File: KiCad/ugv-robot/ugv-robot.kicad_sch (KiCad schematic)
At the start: 16 parts, among them J1 Charging_Port, SW1 LRF, SW2 Zoom_In, SW3 Zoom_Out, SW4 Body_Up, SW5 Body_Down, SW6 Lamp, U1 Analog_Joystick, U2 Digital_Joystick, U3 Boost_Conv, U4 Asus_NUC, U6 Monitor, U7 USB_HUB

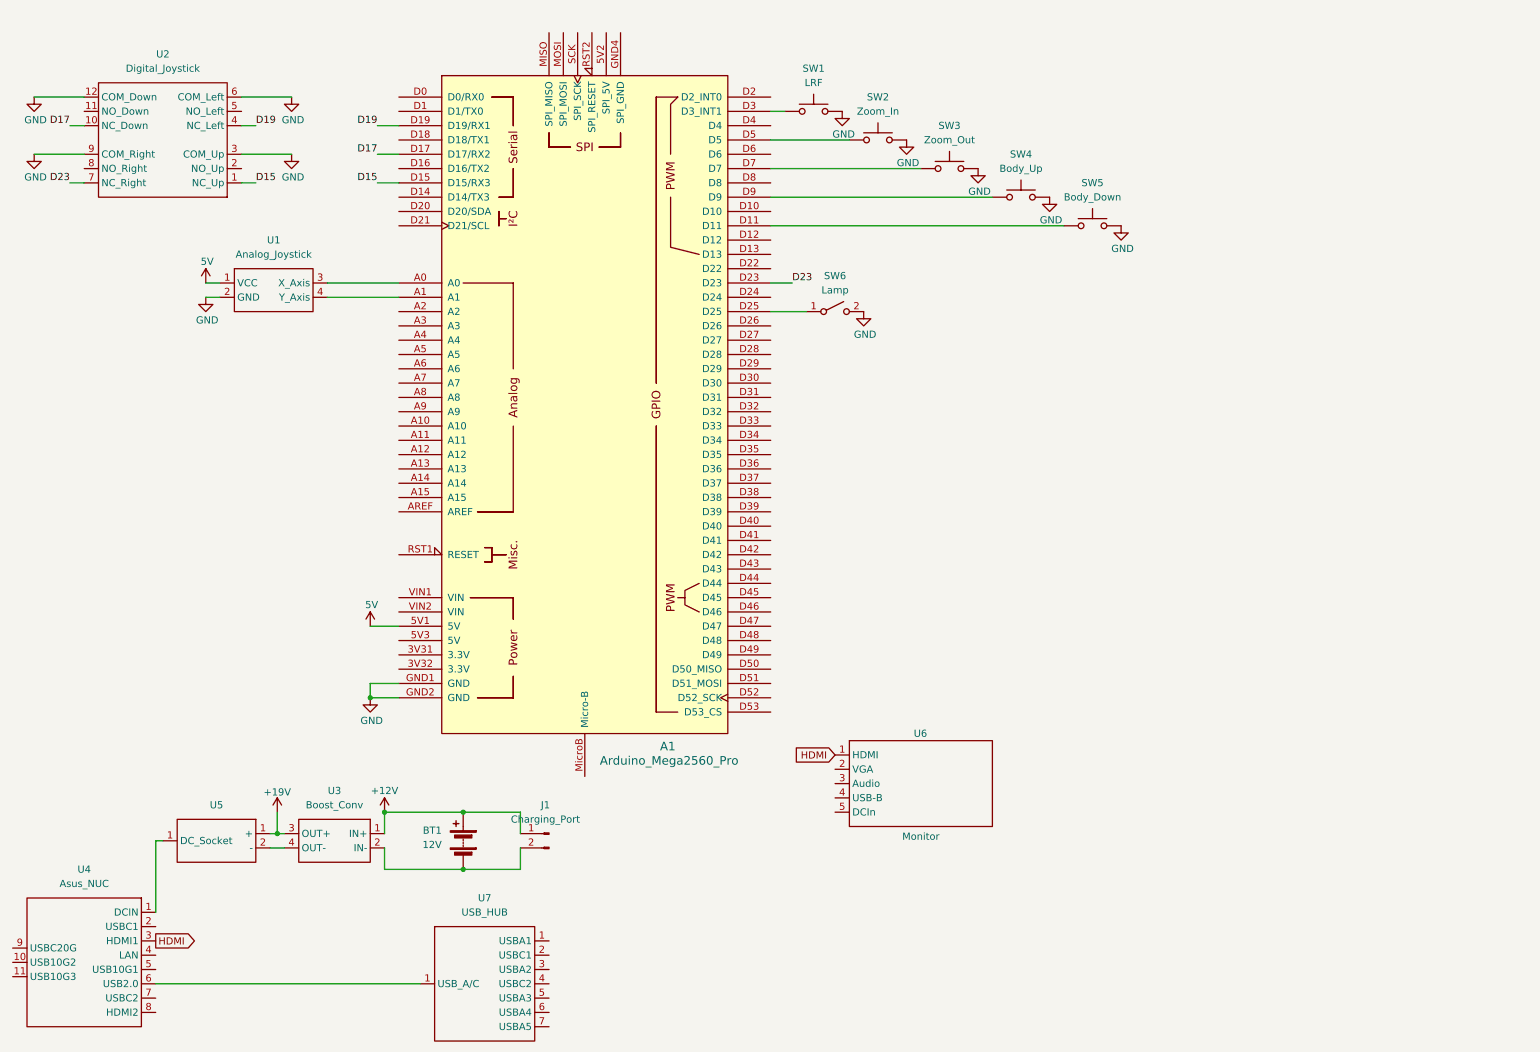
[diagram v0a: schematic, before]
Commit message: Update GCS app, tambah G474 board/hardware, dan STM32 ROS2 interface
Co-Authored-By: Claude Sonnet 5 <noreply@anthropic.com>
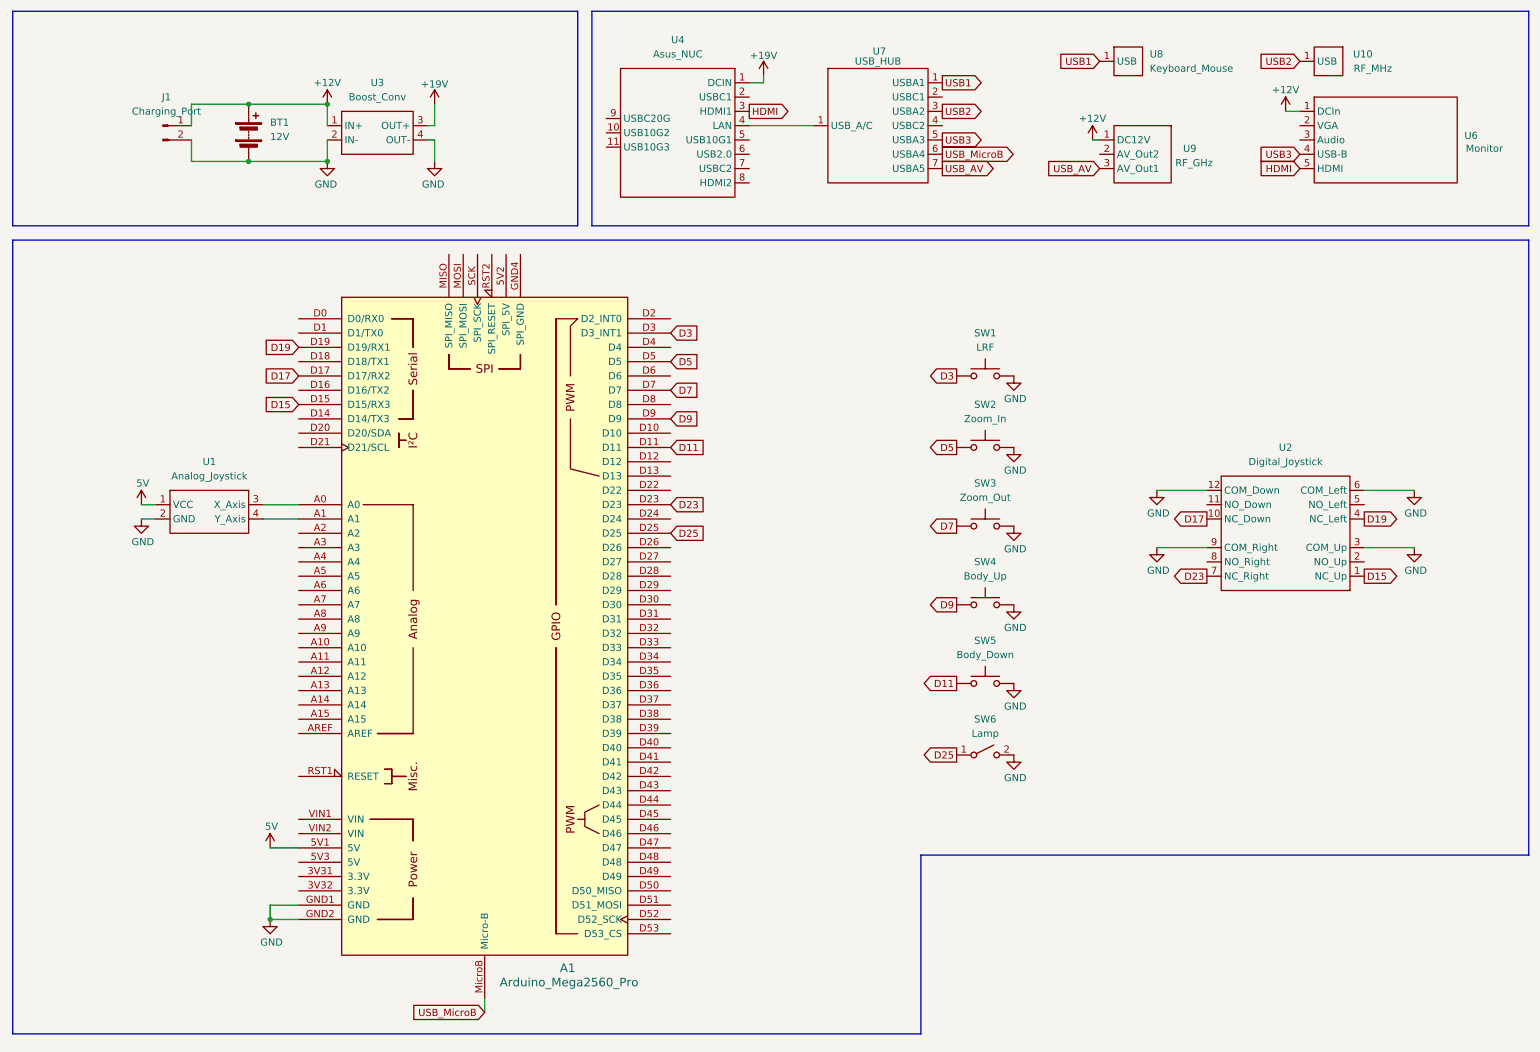
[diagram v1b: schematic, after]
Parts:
- removed U5: (no value), symbol UGV_Lib:DCIn_Converter
- added U10: RF_MHz, symbol UGV_Lib:RF_MHz
- added U8: Keyboard_Mouse, symbol UGV_Lib:Keyboard_Mouse
- added U9: RF_GHz, symbol UGV_Lib:RF_GHz
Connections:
- net +12V: now also U6.1 (DCIn), U9.1 (DC12V)
- net +19V: now also U4.1 (DCIN)
- net GND: now also BT1.2 (-), J1.2 (Pin_2), U3.2 (IN-), U3.4 (OUT-)
- net HDMI: now also U6.5 (HDMI); no longer U6.1 (HDMI)
- net D11: now reaches A1.D11, SW5.1
- net D25: now reaches A1.D25, SW6.1 (A)
- net D3: now reaches A1.D3 (D3_INT1), SW1.2
- net D5: now reaches A1.D5, SW2.1
- net D7: now reaches A1.D7, SW3.1
- net D9: now reaches A1.D9, SW4.1
- net USB_MicroB: now reaches A1.MicroB (Micro-B)
- net USB_MicroB: now also U7.6 (USBA4)
- net at U4.4 (LAN): now also U7.1 (USBA1)
- net at U4.6 (USB2.0): no longer U7.1 (USBA1)
- net USB3: now reaches U6.4 (USB-B)
- net USB3: now also U7.5 (USBA3)
- net USB1: now reaches U7.1 (USBA1)
- net USB1: now also U8.1 (USB)
- net USB2: now reaches U7.3 (USBA2)
- net USB2: now also U10.1 (USB)
- net USB_AV: now reaches U7.7 (USBA5)
- net USB_AV: now also U9.3 (AV_Out1)
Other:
- moved on the sheet: A1, BT1, J1, SW1, SW2, SW3, SW4, SW5, SW6, U1, U2, U3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
